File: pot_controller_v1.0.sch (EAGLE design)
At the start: 30 parts, among them IC10 4051D, IC11 4051D, IC13 4051D, IC2 4051D, IC3 4520D, IC4 4051D, IC5 4051D, IC6 4051D, IC7 4051D, IC8 4051D

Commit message: Fixed routing except for possible inhibit-removal
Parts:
- removed POTS8, POTS9: CONN-IDC-10PS, joakim:CONN-IDC-10PS
- added POTS0, POTS1: CONN-IDC-10PS, joakim:CONN-IDC-10PS
- renumbered POTS11 to POTS7
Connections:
- net +5V: now also POTS0-1.KL, POTS0-2.KL, POTS1-1.KL, POTS1-2.KL; no longer POTS8-1.KL, POTS8-2.KL, POTS9-1.KL, POTS9-2.KL
- net GND: now also POTS0-10.KL, POTS0-9.KL, POTS1-10.KL, POTS1-9.KL; no longer POTS8-10.KL, POTS8-9.KL, POTS9-10.KL, POTS9-9.KL
- net POT0: now also POTS0-3.KL; no longer POTS2-3.KL
- net POT1: now also POTS0-4.KL; no longer POTS2-4.KL
- net POT10: now also POTS1-7.KL; no longer POTS4-7.KL
- net POT11: now also POTS1-8.KL; no longer POTS4-8.KL
- net POT12: now also POTS2-3.KL; no longer POTS6-3.KL
- net POT13: now also POTS2-4.KL; no longer POTS6-4.KL
- net POT14: now also POTS2-5.KL; no longer POTS6-5.KL
- net POT15: now also POTS2-6.KL; no longer POTS6-6.KL
- net POT16: now also POTS2-7.KL; no longer POTS6-7.KL
- net POT17: now also POTS2-8.KL; no longer POTS6-8.KL
- net POT18: now also POTS3-3.KL; no longer POTS8-3.KL
- net POT19: now also POTS3-4.KL; no longer POTS8-4.KL
- net POT2: now also POTS0-5.KL; no longer POTS2-5.KL
- net POT20: now also POTS3-5.KL; no longer POTS8-5.KL
- net POT21: now also POTS3-6.KL; no longer POTS8-6.KL
- net POT22: now also POTS3-7.KL; no longer POTS8-7.KL
- net POT23: now also POTS3-8.KL; no longer POTS8-8.KL
- net POT24: now also POTS4-3.KL; no longer POTS3-3.KL
- net POT25: now also POTS4-4.KL; no longer POTS3-4.KL
- net POT26: now also POTS4-5.KL; no longer POTS3-5.KL
- net POT27: now also POTS4-6.KL; no longer POTS3-6.KL
- net POT28: now also POTS4-7.KL; no longer POTS3-7.KL
- net POT29: now also POTS4-8.KL; no longer POTS3-8.KL
- net POT3: now also POTS0-6.KL; no longer POTS2-6.KL
- net POT36: now also POTS6-3.KL; no longer POTS9-3.KL
- net POT37: now also POTS6-4.KL; no longer POTS9-4.KL
- net POT38: now also POTS6-5.KL; no longer POTS9-5.KL
- net POT39: now also POTS6-6.KL; no longer POTS9-6.KL
- net POT4: now also POTS0-7.KL; no longer POTS2-7.KL
- net POT40: now also POTS6-7.KL; no longer POTS9-7.KL
- net POT41: now also POTS6-8.KL; no longer POTS9-8.KL
- net POT5: now also POTS0-8.KL; no longer POTS2-8.KL
- net POT6: now also POTS1-3.KL; no longer POTS4-3.KL
- net POT7: now also POTS1-4.KL; no longer POTS4-4.KL
- net POT8: now also POTS1-5.KL; no longer POTS4-5.KL
- net POT9: now also POTS1-6.KL; no longer POTS4-6.KL
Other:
- note added: "TODO: Must clock be buffered when connecting multiple cards? TODO: Must inhibit and reset be buffered? What is max fanout? Probably just ground inhibit at least. TODO: Silk + screw holes"
- note removed: "TODO: Must clock be buffered when connecting multiple cards? TODO: Must inhibit and reset be buffered? What is max fanout? Probably just ground inhibit at least."
- moved on the sheet: POTS2-1, POTS2-10, POTS2-2, POTS2-3, POTS2-4, POTS2-5, POTS2-6, POTS2-7, POTS2-8, POTS2-9, POTS3-1, POTS3-10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

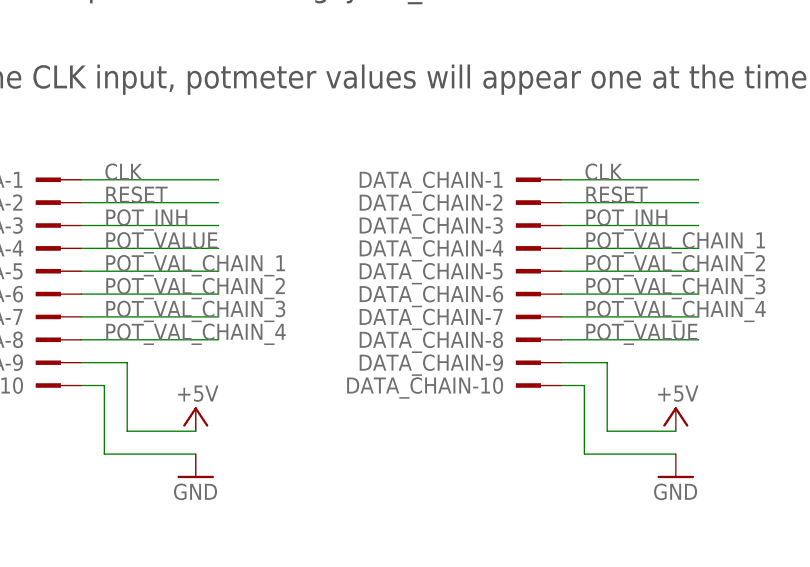
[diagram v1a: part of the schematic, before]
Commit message: Added silk screen
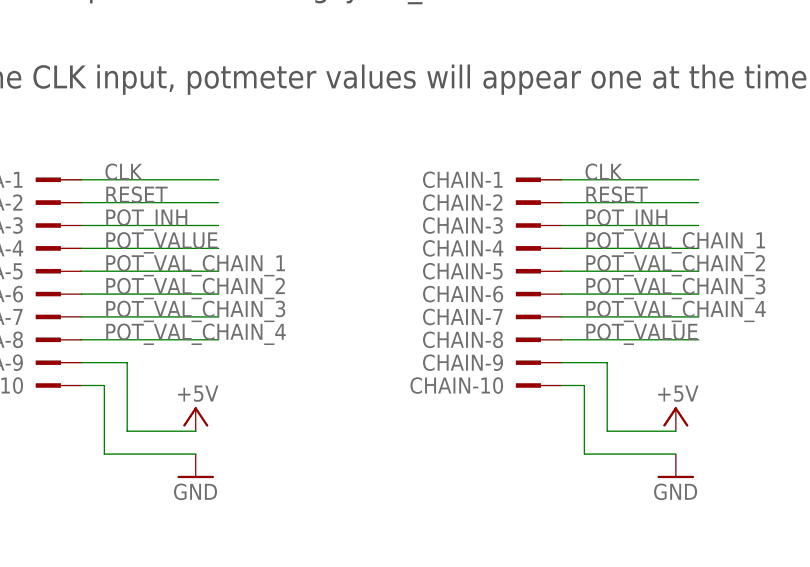
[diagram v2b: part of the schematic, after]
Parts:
- renumbered DATA_CHAIN to CHAIN
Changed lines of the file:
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@@
 <part name="GND26" library="supply1" library_urn="urn:adsk.eagle:library:371" deviceset="GND" device=""/>
 <part name="P+27" library="supply1" library_urn="urn:adsk.eagle:library:371" deviceset="+5V" device=""/>
-<part name="DATA_CHAIN" library="joakim" deviceset="CONN-IDC-10P" device="S" package3d_urn="urn:adsk.eagle:package:5571/1"/>
+<part name="CHAIN" library="joakim" deviceset="CONN-IDC-10P" device="S" package3d_urn="urn:adsk.eagle:package:5571/1"/>
 <part name="GND1" library="supply1" library_urn="urn:adsk.eagle:library:371" deviceset="GND" device=""/>
 <part name="P+4" library="supply1" library_urn="urn:adsk.eagle:library:371" deviceset="+5V" device=""/>
@@
 <attribute name="VALUE" x="104.14" y="-127" size="1.778" layer="96" rot="R180"/>
 </instance>
-<instance part="DATA_CHAIN" gate="-1" x="203.2" y="66.04" smashed="yes">
+<instance part="CHAIN" gate="-1" x="203.2" y="66.04" smashed="yes">
 <attribute name="NAME" x="201.93" y="66.929" size="1.778" layer="95" rot="R180"/>
 </instance>
-<instance part="DATA_CHAIN" gate="-2" x="203.2" y="63.5" smashed="yes">
+<instance part="CHAIN" gate="-2" x="203.2" y="63.5" smashed="yes">
 <attribute name="NAME" x="201.93" y="64.389" size="1.778" layer="95" rot="R180"/>
 </instance>
-<instance part="DATA_CHAIN" gate="-3" x="203.2" y="60.96" smashed="yes">
+<instance part="CHAIN" gate="-3" x="203.2" y="60.96" smashed="yes">
 <attribute name="NAME" x="201.93" y="61.849" size="1.778" layer="95" rot="R180"/>
 </instance>
-<instance part="DATA_CHAIN" gate="-4" x="203.2" y="58.42" smashed="yes">
+<instance part="CHAIN" gate="-4" x="203.2" y="58.42" smashed="yes">
 <attribute name="NAME" x="201.93" y="59.309" size="1.778" layer="95" rot="R180"/>
 </instance>
-<instance part="DATA_CHAIN" gate="-5" x="203.2" y="55.88" smashed="yes">
+<instance part="CHAIN" gate="-5" x="203.2" y="55.88" smashed="yes">
 <attribute name="NAME" x="201.93" y="56.769" size="1.778" layer="95" rot="R180"/>
 </instance>
-<instance part="DATA_CHAIN" gate="-6" x="203.2" y="53.34" smashed="yes">
+<instance part="CHAIN" gate="-6" x="203.2" y="53.34" smashed="yes">
 <attribute name="NAME" x="201.93" y="54.229" size="1.778" layer="95" rot="R180"/>
 </instance>
-<instance part="DATA_CHAIN" gate="-7" x="203.2" y="50.8" smashed="yes">
+<instance part="CHAIN" gate="-7" x="203.2" y="50.8" smashed="yes">
 <attribute name="NAME" x="201.93" y="51.689" size="1.778" layer="95" rot="R180"/>
 </instance>
-<instance part="DATA_CHAIN" gate="-8" x="203.2" y="48.26" smashed="yes">
+<instance part="CHAIN" gate="-8" x="203.2" y="48.26" smashed="yes">
 <attribute name="NAME" x="201.93" y="49.149" size="1.778" layer="95" rot="R180"/>
 </instance>
-<instance part="DATA_CHAIN" gate="-9" x="203.2" y="45.72" smashed="yes">
+<instance part="CHAIN" gate="-9" x="203.2" y="45.72" smashed="yes">
 <attribute name="NAME" x="201.93" y="46.609" size="1.778" layer="95" rot="R180"/>
 </instance>
-<instance part="DATA_CHAIN" gate="-10" x="203.2" y="43.18" smashed="yes">
+<instance part="CHAIN" gate="-10" x="203.2" y="43.18" smashed="yes">
 <attribute name="NAME" x="201.93" y="44.069" size="1.778" layer="95" rot="R180"/>
 </instance>
@@
 </segment>
 <segment>
-<pinref part="DATA_CHAIN" gate="-9" pin="KL"/>
+<pinref part="CHAIN" gate="-9" pin="KL"/>
 <wire x1="220.98" y1="38.1" x2="213.36" y2="38.1" width="0.1524" layer="91"/>
 <wire x1="213.36" y1="38.1" x2="213.36" y2="45.72" width="0.1524" layer="91"/>
@@
 </segment>
 <segment>
-<pinref part="DATA_CHAIN" gate="-10" pin="KL"/>
+<pinref part="CHAIN" gate="-10" pin="KL"/>
 <wire x1="208.28" y1="43.18" x2="210.82" y2="43.18" width="0.1524" layer="91"/>
 <wire x1="210.82" y1="43.18" x2="210.82" y2="35.56" width="0.1524" layer="91"/>
@@
 </segment>
 <segment>
-<pinref part="DATA_CHAIN" gate="-8" pin="KL"/>
+<pinref part="CHAIN" gate="-8" pin="KL"/>
 <wire x1="208.28" y1="48.26" x2="223.52" y2="48.26" width="0.1524" layer="91"/>
 <label x="210.82" y="48.26" size="1.778" layer="95"/>
@@
 </segment>
 <segment>
-<pinref part="DATA_CHAIN" gate="-1" pin="KL"/>
+<pinref part="CHAIN" gate="-1" pin="KL"/>
 <wire x1="208.28" y1="66.04" x2="223.52" y2="66.04" width="0.1524" layer="91"/>
 <label x="210.82" y="66.04" size="1.778" layer="95"/>
@@
 </segment>
 <segment>
-<pinref part="DATA_CHAIN" gate="-2" pin="KL"/>
+<pinref part="CHAIN" gate="-2" pin="KL"/>
 <wire x1="223.52" y1="63.5" x2="208.28" y2="63.5" width="0.1524" layer="91"/>
 <label x="210.82" y="63.5" size="1.778" layer="95"/>
@@
 </segment>
 <segment>
-<pinref part="DATA_CHAIN" gate="-3" pin="KL"/>
+<pinref part="CHAIN" gate="-3" pin="KL"/>
 <wire x1="208.28" y1="60.96" x2="223.52" y2="60.96" width="0.1524" layer="91"/>
 <label x="210.82" y="60.96" size="1.778" layer="95"/>
@@
 </segment>
 <segment>
-<pinref part="DATA_CHAIN" gate="-4" pin="KL"/>
+<pinref part="CHAIN" gate="-4" pin="KL"/>
 <wire x1="208.28" y1="58.42" x2="223.52" y2="58.42" width="0.1524" layer="91"/>
 <label x="210.82" y="58.42" size="1.778" layer="95"/>
@@
 </segment>
 <segment>
-<pinref part="DATA_CHAIN" gate="-6" pin="KL"/>
+<pinref part="CHAIN" gate="-6" pin="KL"/>
 <wire x1="223.52" y1="53.34" x2="208.28" y2="53.34" width="0.1524" layer="91"/>
 <label x="210.82" y="53.34" size="1.778" layer="95"/>
@@
 </segment>
 <segment>
-<pinref part="DATA_CHAIN" gate="-7" pin="KL"/>
+<pinref part="CHAIN" gate="-7" pin="KL"/>
 <wire x1="208.28" y1="50.8" x2="223.52" y2="50.8" width="0.1524" layer="91"/>
 <label x="210.82" y="50.8" size="1.778" layer="95"/>
@@
 </segment>
 <segment>
-<pinref part="DATA_CHAIN" gate="-5" pin="KL"/>
+<pinref part="CHAIN" gate="-5" pin="KL"/>
 <wire x1="208.28" y1="55.88" x2="223.52" y2="55.88" width="0.1524" layer="91"/>
 <label x="210.82" y="55.88" size="1.778" layer="95"/>

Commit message: Updated IDC connector
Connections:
- removed net POT_INH: CHAIN-3.KL, DATA-3.KL, IC10A.INH, IC11A.INH, IC13A.INH, IC2A.INH, IC4A.INH, IC5A.INH, IC6A.INH, IC7A.INH, IC8A.INH
- new net POT_VAL_CHAIN_5: CHAIN-7.KL, DATA-8.KL
- net GND: now also IC10A.INH, IC11A.INH, IC13A.INH, IC2A.INH, IC4A.INH, IC5A.INH, IC6A.INH, IC7A.INH, IC8A.INH
- net POT_VALUE: now also DATA-3.KL; no longer DATA-4.KL
- net POT_VAL_CHAIN_1: now also CHAIN-3.KL, DATA-4.KL; no longer CHAIN-4.KL, DATA-5.KL
- net POT_VAL_CHAIN_2: now also CHAIN-4.KL, DATA-5.KL; no longer CHAIN-5.KL, DATA-6.KL
- net POT_VAL_CHAIN_3: now also CHAIN-5.KL, DATA-6.KL; no longer CHAIN-6.KL, DATA-7.KL
- net POT_VAL_CHAIN_4: now also CHAIN-6.KL, DATA-7.KL; no longer CHAIN-7.KL, DATA-8.KL
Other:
- note added: "TODO: Must clock be buffered when connecting multiple cards? TODO: Must reset be buffered? What is max fanout?"
- note added: "When clocking the CLK input, potmeter values will appear one at the time on the value output Can be run at around 50kS per second, speed is limited by the ADC on the Teensy"
- note removed: "TODO: Must clock be buffered when connecting multiple cards? TODO: Must inhibit and reset be buffered? What is max fanout? Probably just ground inhibit at least. TODO: Silk + screw holes"
- note removed: "When clocking the CLK input, potmeter values will appear one at the time on the value output"
- note removed: "http://musicfromouterspace.com/analogsynth_new/OLDIESBUTGOODIES/CONTROLLERS/scanningmatrixkeyboard.html"
- moved on the sheet: C1, C2, CHAIN-1, CHAIN-10, CHAIN-2, CHAIN-3, CHAIN-4, CHAIN-5, CHAIN-6, CHAIN-7, CHAIN-8, CHAIN-9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
